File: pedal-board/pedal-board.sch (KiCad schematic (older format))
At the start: 42 parts, among them J1 AudioJack0, J2 AudioJack1, J3 AudioJack2, J4 AudioJack3, J5 SPI, U1 MCP3004

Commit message: Convert pedal board over to I2C/Qwiic. Adjust mounting hole spacing.
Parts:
- removed J5: SPI, Pin_Headers:Pin_Header_Angled_1x06_Pitch2.54mm, symbol Connector:Conn_01x06_Male
- removed U1: MCP3004, Housings_SSOP:SSOP-14_5.3x6.2mm_Pitch0.65mm, symbol Analog_ADC:MCP3004
- added J5: Qwiic, Connectors_JST:JST_SH_SM04B-SRSS-TB_04x1.00mm_Angled, symbol Connector:Conn_01x04_Female
- added U1: ADS7830, Housings_SSOP:TSSOP-16_4.4x5mm_Pitch0.65mm, symbol Analog_DAC:ADS7830
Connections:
- net labels added: SCL, SDA
- wire segments 148 -> 138
- no-connect marks 0 -> 4
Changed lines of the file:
@@
 $EndDescr
-$Comp
-L Analog_ADC:MCP3004 U1
-U 1 1 5FD36C85
-P 7600 2350
-F 0 "U1" H 8000 2850 50  0000 C CNN
-F 1 "MCP3004" H 8000 2750 50  0000 C CNN
-F 2 "Housings_SSOP:SSOP-14_5.3x6.2mm_Pitch0.65mm" H 8500 2050 50  0001 C CNN
-F 3 "http://ww1.microchip.com/downloads/en/DeviceDoc/21295C.pdf" H 8500 2050 50  0001 C CNN
-	1    7600 2350
-	1    0    0    -1
-$EndComp
 $Comp
 L power:GND #PWR04
 U 1 1 5FD37B78
-P 7550 3050
-F 0 "#PWR04" H 7550 2800 50  0001 C CNN
-F 1 "GND" H 7555 2877 50  0000 C CNN
-F 2 "" H 7550 3050 50  0001 C CNN
-F 3 "" H 7550 3050 50  0001 C CNN
-	1    7550 3050
+P 8100 3750
+F 0 "#PWR04" H 8100 3500 50  0001 C CNN
+F 1 "GND" H 8105 3577 50  0000 C CNN
+F 2 "" H 8100 3750 50  0001 C CNN
+F 3 "" H 8100 3750 50  0001 C CNN
+	1    8100 3750
 	1    0    0    -1
 $EndComp
@@
 L power:+3.3V #PWR03
 U 1 1 5FD37E4D
-P 7550 1700
-F 0 "#PWR03" H 7550 1550 50  0001 C CNN
-F 1 "+3.3V" H 7565 1873 50  0000 C CNN
-F 2 "" H 7550 1700 50  0001 C CNN
-F 3 "" H 7550 1700 50  0001 C CNN
-	1    7550 1700
-	1    0    0    -1
-$EndComp
-Wire Wire Line
-	7500 1950 7500 1800
-Wire Wire Line
-	7500 1800 7550 1800
-Wire Wire Line
-	7600 1800 7600 1950
-Wire Wire Line
-	7550 1700 7550 1800
-Connection ~ 7550 1800
-Wire Wire Line
-	7550 1800 7600 1800
-Wire Wire Line
-	7500 2850 7500 2950
-Wire Wire Line
-	7500 2950 7550 2950
-Wire Wire Line
-	7600 2950 7600 2850
-Wire Wire Line
-	7550 3050 7550 2950
-Connection ~ 7550 2950
-Wire Wire Line
-	7550 2950 7600 2950
+P 8100 2350
+F 0 "#PWR03" H 8100 2200 50  0001 C CNN
+F 1 "+3.3V" H 8115 2523 50  0000 C CNN
+F 2 "" H 8100 2350 50  0001 C CNN
+F 3 "" H 8100 2350 50  0001 C CNN
+	1    8100 2350
+	1    0    0    -1
+$EndComp
 $Comp
 L Connector:AudioJack3 J1
@@
 $EndComp
 Wire Wire Line
-	7000 2250 6500 2250
-Wire Wire Line
-	7000 2350 6500 2350
-Wire Wire Line
-	7000 2450 6500 2450
-Wire Wire Line
-	7000 2550 6500 2550
-Text Label 6500 2250 0    50   ~ 0
+	7600 2650 7100 2650
+Wire Wire Line
+	7600 2750 7100 2750
+Wire Wire Line
+	7600 2850 7100 2850
+Wire Wire Line
+	7600 2950 7100 2950
+Text Label 7100 2650 0    50   ~ 0
 CH0
-Text Label 6500 2350 0    50   ~ 0
+Text Label 7100 2750 0    50   ~ 0
 CH1
-Text Label 6500 2450 0    50   ~ 0
+Text Label 7100 2850 0    50   ~ 0
 CH2
-Text Label 6500 2550 0    50   ~ 0
+Text Label 7100 2950 0    50   ~ 0
 CH3
 $Comp
@@
 	4250 3450 4250 3650
 $Comp
-L Connector:Conn_01x06_Male J5
-U 1 1 5FDCD81D
-P 9450 2450
-F 0 "J5" H 9422 2332 50  0000 R CNN
-F 1 "SPI" H 9422 2423 50  0000 R CNN
-F 2 "Pin_Headers:Pin_Header_Angled_1x06_Pitch2.54mm" H 9450 2450 50  0001 C CNN
-F 3 "~" H 9450 2450 50  0001 C CNN
-	1    9450 2450
-	-1   0    0    1
-$EndComp
-$Comp
 L power:+3.3V #PWR0107
 U 1 1 5FDCEDC2
-P 9100 2050
-F 0 "#PWR0107" H 9100 1900 50  0001 C CNN
-F 1 "+3.3V" H 9115 2223 50  0000 C CNN
-F 2 "" H 9100 2050 50  0001 C CNN
-F 3 "" H 9100 2050 50  0001 C CNN
-	1    9100 2050
+P 9500 2850
+F 0 "#PWR0107" H 9500 2700 50  0001 C CNN
+F 1 "+3.3V" H 9515 3023 50  0000 C CNN
+F 2 "" H 9500 2850 50  0001 C CNN
+F 3 "" H 9500 2850 50  0001 C CNN
+	1    9500 2850
 	1    0    0    -1
 $EndComp
@@
 L power:GND #PWR0108
 U 1 1 5FDCF69F
-P 9100 2750
-F 0 "#PWR0108" H 9100 2500 50  0001 C CNN
-F 1 "GND" H 9105 2577 50  0000 C CNN
-F 2 "" H 9100 2750 50  0001 C CNN
-F 3 "" H 9100 2750 50  0001 C CNN
-	1    9100 2750
-	1    0    0    -1
-$EndComp
-Wire Wire Line
-	9100 2750 9100 2650
-Wire Wire Line
-	9100 2650 9250 2650
-Wire Wire Line
-	9100 2050 9100 2150
-Wire Wire Line
-	9100 2150 9250 2150
+P 9500 3100
+F 0 "#PWR0108" H 9500 2850 50  0001 C CNN
+F 1 "GND" H 9505 2927 50  0000 C CNN
+F 2 "" H 9500 3100 50  0001 C CNN
+F 3 "" H 9500 3100 50  0001 C CNN
+	1    9500 3100
+	1    0    0    -1
+$EndComp
 $Comp
 L Device:C_Small C1
@@
 	1    0    0    -1
 $EndComp
-Wire Wire Line
-	8200 2250 8350 2250
-Wire Wire Line
-	8350 2250 8450 2550
-Wire Wire Line
-	8450 2550 9250 2550
-Wire Wire Line
-	8200 2550 8350 2550
-Wire Wire Line
-	8350 2550 8450 2250
-Wire Wire Line
-	8450 2250 9250 2250
-Wire Wire Line
-	8200 2350 8500 2350
-Wire Wire Line
-	8500 2350 8550 2450
-Wire Wire Line
-	8550 2450 9250 2450
-Wire Wire Line
-	8200 2450 8500 2450
-Wire Wire Line
-	8500 2450 8550 2350
-Wire Wire Line
-	8550 2350 9250 2350
+$Comp
+L Analog_DAC:ADS7830 U1
+U 1 1 5FD6C453
+P 8100 3050
+F 0 "U1" H 8300 3700 50  0000 C CNN
+F 1 "ADS7830" H 8350 3600 50  0000 C CNN
+F 2 "Housings_SSOP:TSSOP-16_4.4x5mm_Pitch0.65mm" H 8200 2350 50  0001 C CIN
+F 3 "http://www.ti.com/lit/ds/symlink/ads7830.pdf" H 8300 2600 50  0001 C CNN
+	1    8100 3050
+	1    0    0    -1
+$EndComp
+NoConn ~ 7600 3050
+NoConn ~ 7600 3150
+NoConn ~ 7600 3250
+NoConn ~ 7600 3350
+Wire Wire Line
+	8100 2350 8100 2450
+Wire Wire Line
+	8100 3750 8100 3700
+Wire Wire Line
+	8100 3700 8700 3700
+Wire Wire Line
+	8700 3700 8700 3350
+Wire Wire Line
+	8700 3250 8600 3250
+Connection ~ 8100 3700
+Wire Wire Line
+	8100 3700 8100 3650
+Wire Wire Line
+	8600 3350 8700 3350
+Connection ~ 8700 3350
+Wire Wire Line
+	8700 3350 8700 3250
+Wire Wire Line
+	8600 2650 9000 2650
+Wire Wire Line
+	8600 2750 9000 2750
+Text Label 9000 2750 2    50   ~ 0
+SCL
+Text Label 9000 2650 2    50   ~ 0
+SDA
+$Comp
+L Connector:Conn_01x04_Female J5
+U 1 1 5FDB53D4
+P 10250 2900
+F 0 "J5" H 10142 2475 50  0000 C CNN
+F 1 "Qwiic" H 10142 2566 50  0000 C CNN
+F 2 "Connectors_JST:JST_SH_SM04B-SRSS-TB_04x1.00mm_Angled" H 10250 2900 50  0001 C CNN
+F 3 "~" H 10250 2900 50  0001 C CNN
+	1    10250 2900
+	1    0    0    1
+$EndComp
+Wire Wire Line
+	9500 2850 9500 2900
+Wire Wire Line
+	9500 2900 10050 2900
+Wire Wire Line
+	10050 3000 9500 3000
+Wire Wire Line
+	9500 3000 9500 3100
+Wire Wire Line
+	10050 2800 9650 2800
+Wire Wire Line
+	10050 2700 9650 2700
+Text Label 9650 2700 0    50   ~ 0
+SCL
+Text Label 9650 2800 0    50   ~ 0
+SDA
 $EndSCHEMATC

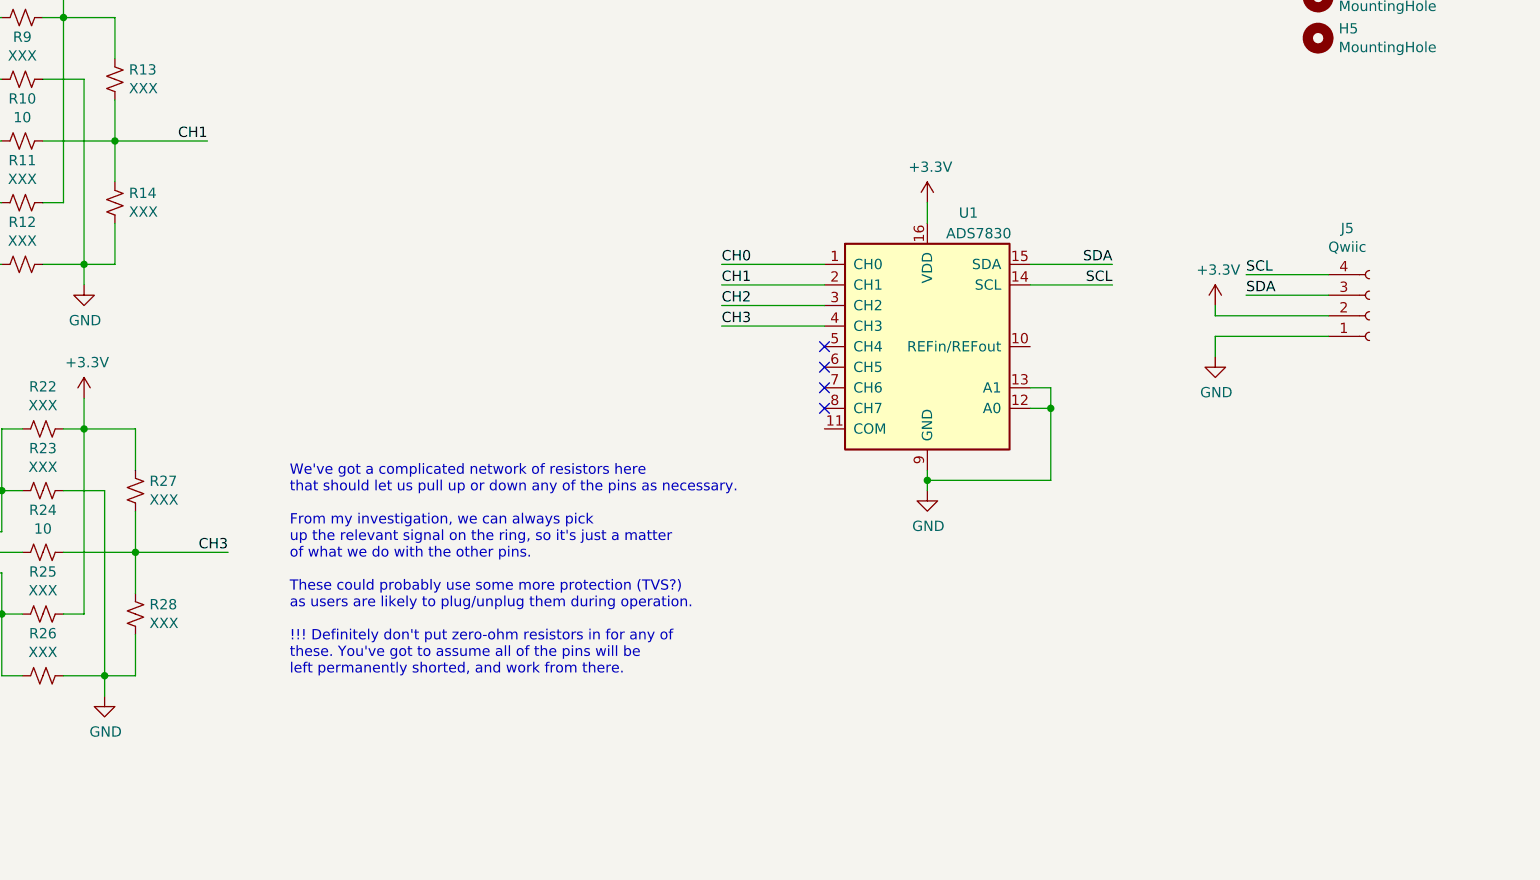
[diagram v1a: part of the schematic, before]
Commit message: Complete pedal board I2C conversion; make I2C address configurable.
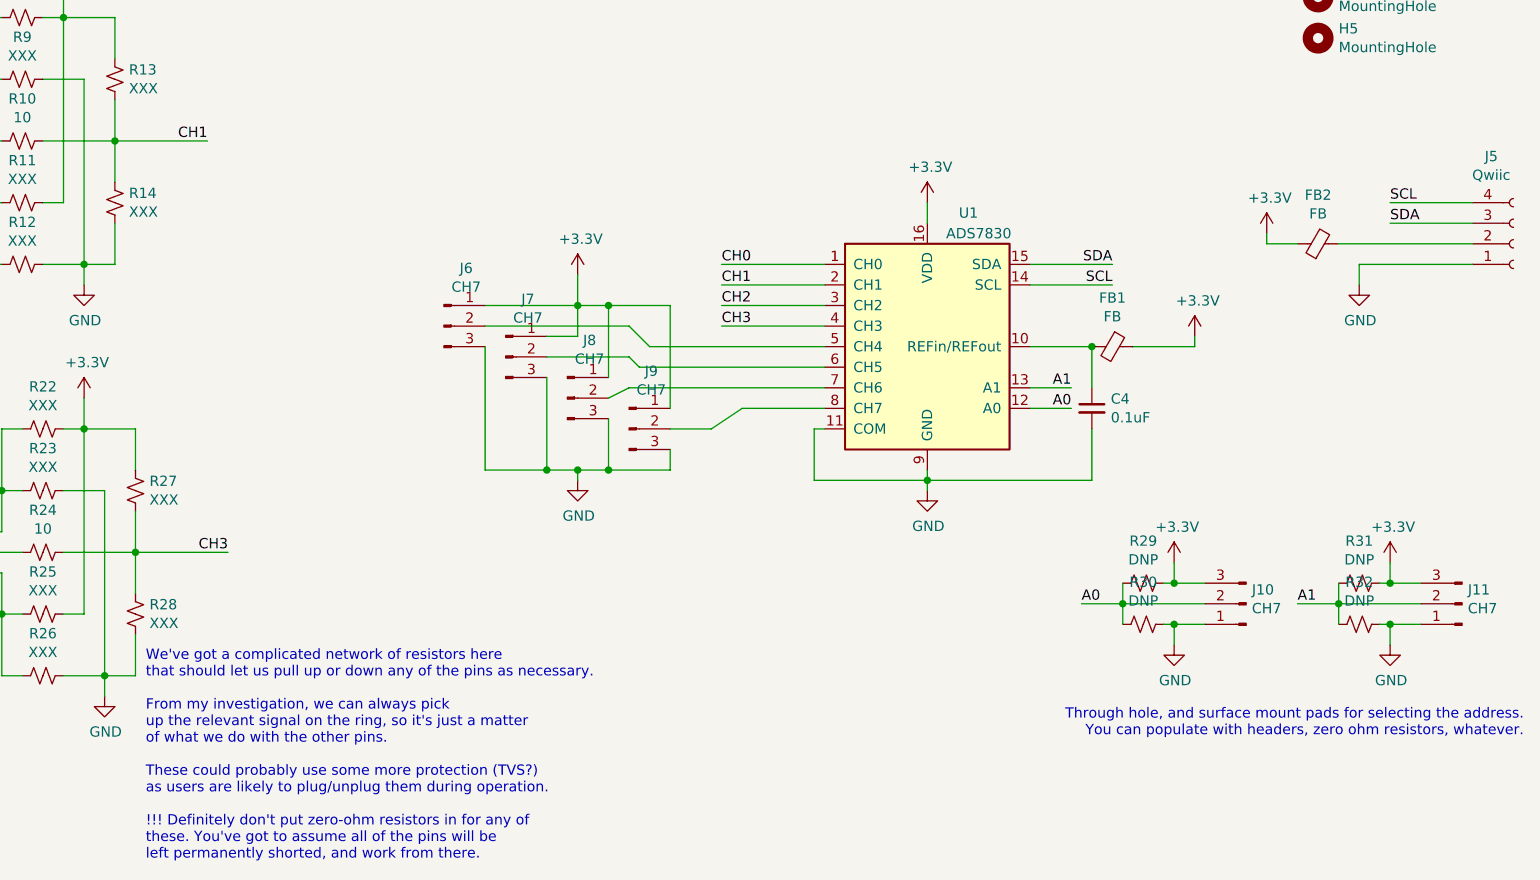
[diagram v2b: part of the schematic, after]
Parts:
- added C4: 0.1uF, Capacitors_SMD:C_0805_HandSoldering, symbol Device:C_Small
- added FB1, FB2: FB, Inductors_SMD:L_0805_HandSoldering, symbol Device:Ferrite_Bead_Small
- added J10, J11, J6, J7, J8, J9: CH7, Pin_Headers:Pin_Header_Straight_1x03_Pitch2.54mm, symbol Connector:Conn_01x03_Male
- added R29, R30, R31, R32: DNP, Resistors_SMD:R_0805_HandSoldering, symbol Device:R_Small_US
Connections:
- net +3V3: now also FB1.1, FB2.1, J10.3 (Pin_3), J11.3 (Pin_3), J6.1 (Pin_1), J7.1 (Pin_1), J8.1 (Pin_1), J9.1 (Pin_1), R29.1, R31.1; no longer J5.2 (Pin_2)
- net GND: now also U1.11 (COM), C4.2, J10.1 (Pin_1), J11.1 (Pin_1), J6.3 (Pin_3), J7.3 (Pin_3), J8.3 (Pin_3), J9.3 (Pin_3), R30.1, R32.1; no longer U1.12 (A0), U1.13 (A1)
- net at U1.10 (REFin/REFout): now also C4.1, FB1.2
- net at U1.5 (CH4): now also J6.2 (Pin_2)
- net at U1.6 (CH5): now also J7.2 (Pin_2)
- net at U1.7 (CH6): now also J8.2 (Pin_2)
- net at U1.8 (CH7): now also J9.2 (Pin_2)
- new net: FB2.2, J5.2 (Pin_2)
- new net A0: J10.2 (Pin_2), R29.2, R30.2, U1.12 (A0)
- new net A1: J11.2 (Pin_2), R31.2, R32.2, U1.13 (A1)
- no-connect marks 4 -> 0
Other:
- note added: "Through hole, and surface mount pads for selecting the address.\nYou can populate with headers, zero ohm resistors, whatever."
- moved on the sheet: J5
